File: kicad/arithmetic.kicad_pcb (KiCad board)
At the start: 4 copper layers, 47.3 x 58.3 mm, 72 parts, among them J1 Conn_01x03_Male, J2 Conn_01x05_Male, J3 Conn_01x05_Male, J4 Conn_Coaxial, J5 Conn_Coaxial, J6 Conn_Coaxial, M2.5 MountingHole_2.7mm_M2.5_ISO73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, U1 LM317, U2 LM337, U3 OPA197xDBV, U4 OPA197xDBV, U5 OPA197xDBV

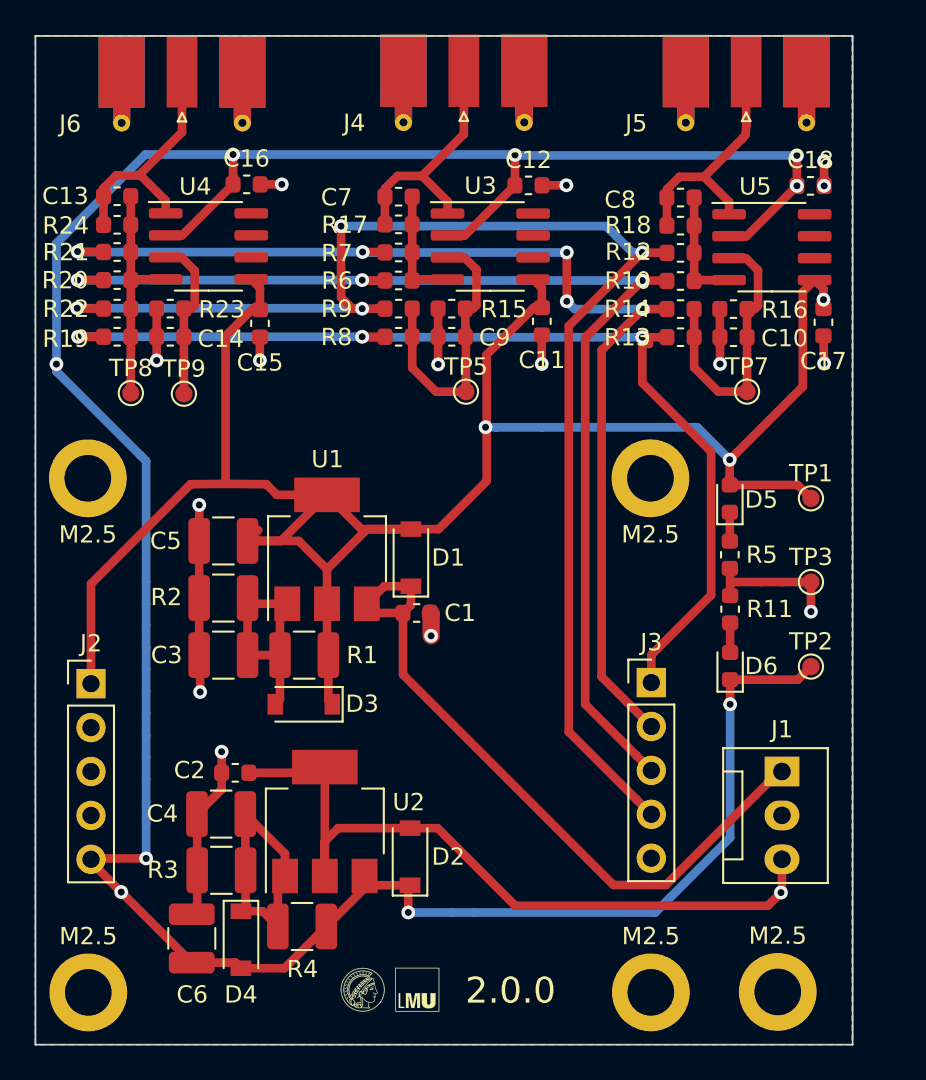
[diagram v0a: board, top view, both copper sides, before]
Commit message: fixed signal routing, remaining vias, large traces
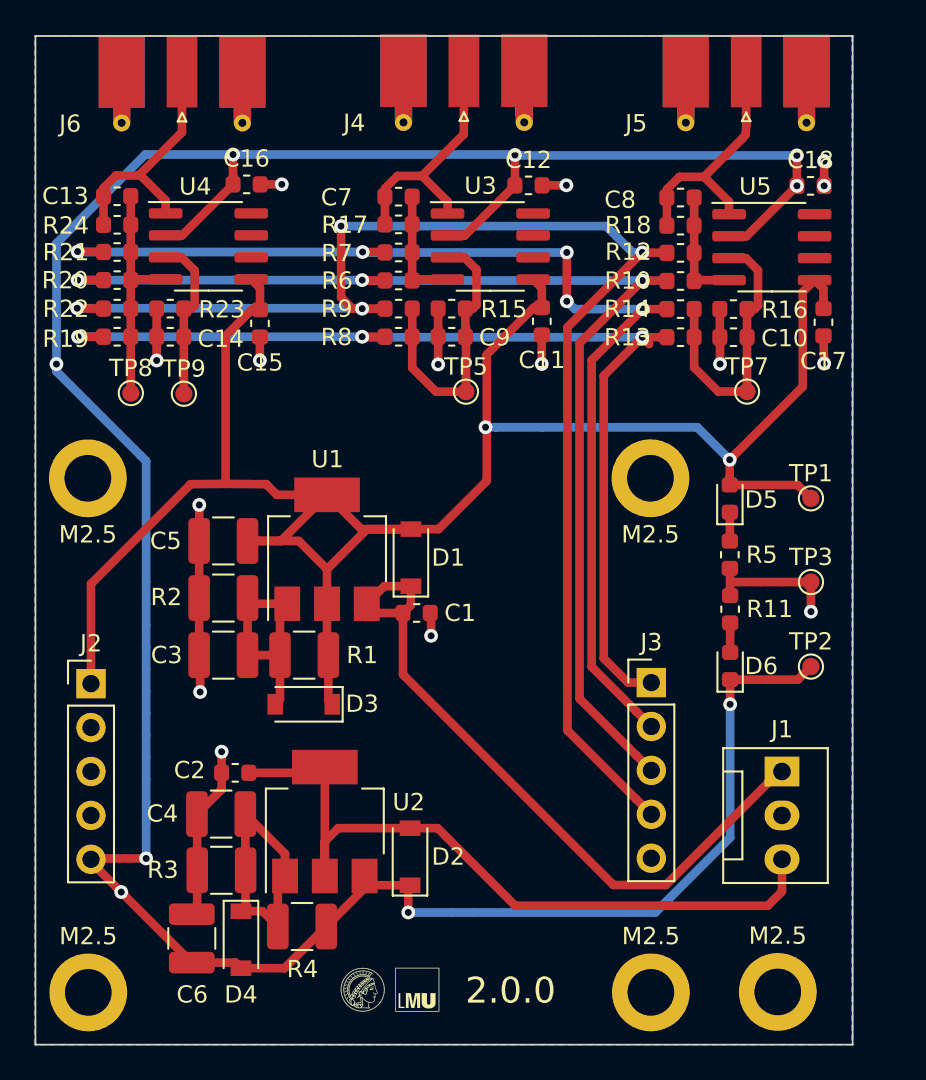
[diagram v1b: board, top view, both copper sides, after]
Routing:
- net +12V: track 121.3 -> 120.4 mm, vias 3 -> 2
- net -15V: vias 1 -> 0
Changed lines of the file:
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@@
     (thickness 1.6)
     (drawings 8)
-    (tracks 420)
+    (tracks 416)
     (zones 0)
     (modules 72)
@@
   )
   (setup
-    (last_trace_width 0.25)
+    (last_trace_width 0.5)
     (user_trace_width 0.5)
     (user_trace_width 0.75)
@@
   (segment (start 119.3806 86.1654) (end 119.3806 84.735) (width 0.5) (layer F.Cu) (net 1))
   (via (at 96.647 112.1918) (size 0.8) (drill 0.4) (layers F.Cu B.Cu) (net 1))
-  (segment (start 96.647 110.9217) (end 96.5963 110.871) (width 1) (layer F.Cu) (net 1))
-  (segment (start 96.647 112.1918) (end 96.647 110.9217) (width 1) (layer F.Cu) (net 1))
+  (segment (start 96.647 112.1918) (end 96.647 110.9217) (width 0.5) (layer F.Cu) (net 1))
+  (segment (start 96.647 110.9217) (end 96.5963 110.871) (width 0.5) (layer F.Cu) (net 1))
   (segment (start 119.3431 94.8429) (end 119.38 96.4438) (width 0.5) (layer F.Cu) (net 1))
   (segment (start 119.38 96.4438) (end 119.3431 96.4069) (width 0.5) (layer F.Cu) (net 1))
@@
   (segment (start 95.4278 123.318) (end 97.0278 123.318) (width 0.5) (layer F.Cu) (net 3))
   (segment (start 116.8835 127.0435) (end 116.9416 126.9854) (width 0.5) (layer F.Cu) (net 3))
-  (via (at 116.8835 127.0435) (size 0.8) (drill 0.4) (layers F.Cu B.Cu) (net 3))
   (segment (start 86.3608 110.3384) (end 86.0298 110.0074) (width 0.5) (layer F.Cu) (net 4))
   (segment (start 88.3272 110.3384) (end 86.3608 110.3384) (width 0.5) (layer F.Cu) (net 4))
@@
   (segment (start 90.7064 115.9296) (end 90.931 116.1542) (width 0.5) (layer F.Cu) (net 6))
   (segment (start 90.7064 113.3094) (end 90.7064 115.9296) (width 0.5) (layer F.Cu) (net 6))
-  (segment (start 86.0298 106.7054) (end 86.6548 106.0804) (width 0.5) (layer F.Cu) (net 6))
   (segment (start 86.6548 106.7054) (end 86.0298 106.7054) (width 0.5) (layer F.Cu) (net 6))
   (segment (start 88.9942 106.7054) (end 86.6548 106.7054) (width 0.5) (layer F.Cu) (net 6))
@@
   (segment (start 118.8324 91.6178) (end 118.143091 92.307109) (width 0.5) (layer F.Cu) (net 6))
   (segment (start 119.3431 92.7469) (end 119.3431 92.1285) (width 0.5) (layer F.Cu) (net 6))
-  (via (at 119.3431 92.7469) (size 0.8) (drill 0.4) (layers F.Cu B.Cu) (net 6))
   (segment (start 103.070601 100.129399) (end 100.403601 100.129399) (width 0.5) (layer B.Cu) (net 6))
   (segment (start 82.245 89.027) (end 81.2942 89.027) (width 0.5) (layer F.Cu) (net 7))
@@
   (segment (start 79.847716 85.56639) (end 78.42341 85.56639) (width 0.5) (layer F.Cu) (net 13))
   (segment (start 81.2942 87.757) (end 81.2942 87.012874) (width 0.5) (layer F.Cu) (net 13))
-  (segment (start 82.2392 79.54) (end 82.2392 83.064) (width 0.5) (layer F.Cu) (net 13) (status 1000000))
-  (segment (start 82.2392 83.064) (end 79.847716 85.455484) (width 0.5) (layer F.Cu) (net 13) (status 1000000))
-  (segment (start 79.847716 85.455484) (end 79.847716 85.56639) (width 0.5) (layer F.Cu) (net 13) (status 1000000))
+  (segment (start 82.2392 79.54) (end 82.2392 83.064) (width 0.5) (layer F.Cu) (net 13))
+  (segment (start 82.2392 83.064) (end 79.847716 85.455484) (width 0.5) (layer F.Cu) (net 13))
+  (segment (start 79.847716 85.455484) (end 79.847716 85.56639) (width 0.5) (layer F.Cu) (net 13))
   (segment (start 82.347 93.2688) (end 82.347 94.8944) (width 0.5) (layer F.Cu) (net 14))
   (segment (start 82.96921 93.08409) (end 82.7845 93.2688) (width 0.5) (layer F.Cu) (net 14))
@@
   (segment (start 108.8644 90.0176) (end 108.8898 90.043) (width 0.5) (layer F.Cu) (net 17))
   (via (at 108.8644 90.0176) (size 0.8) (drill 0.4) (layers F.Cu B.Cu) (net 17))
-  (segment (start 108.535101 121.666901) (end 109.3851 122.5169) (width 0.5) (layer F.Cu) (net 17))
-  (segment (start 104.609279 94.272721) (end 104.609279 117.741079) (width 0.5) (layer F.Cu) (net 17))
-  (segment (start 104.609279 117.741079) (end 108.535101 121.666901) (width 0.5) (layer F.Cu) (net 17))
-  (segment (start 108.8644 90.0176) (end 104.609279 94.272721) (width 0.5) (layer F.Cu) (net 17))
   (segment (start 93.9799 93.2688) (end 93.5424 93.2688) (width 0.5) (layer F.Cu) (net 17))
   (segment (start 93.5424 93.2688) (end 92.6592 93.2688) (width 0.5) (layer F.Cu) (net 17))
@@
   (segment (start 92.093515 93.2688) (end 92.6592 93.2688) (width 0.5) (layer F.Cu) (net 17))
   (segment (start 91.44 88.4936) (end 91.44 92.615285) (width 0.5) (layer F.Cu) (net 17))
+  (segment (start 108.535101 121.666901) (end 109.3851 122.5169) (width 0.5) (layer F.Cu) (net 17))
+  (segment (start 104.534269 117.666069) (end 108.535101 121.666901) (width 0.5) (layer F.Cu) (net 17))
+  (segment (start 104.534269 94.347731) (end 104.534269 117.666069) (width 0.5) (layer F.Cu) (net 17))
+  (segment (start 108.8644 90.0176) (end 104.534269 94.347731) (width 0.5) (layer F.Cu) (net 17))
   (segment (start 77.6985 89.9922) (end 76.2 89.9668) (width 0.5) (layer F.Cu) (net 18))
   (segment (start 76.2 89.9668) (end 76.2254 89.9922) (width 0.5) (layer F.Cu) (net 18))
@@
   (segment (start 108.8898 93.2942) (end 108.8898 93.2942) (width 0.5) (layer F.Cu) (net 18))
   (via (at 108.8898 93.2942) (size 0.8) (drill 0.4) (layers F.Cu B.Cu) (net 18))
-  (segment (start 108.489801 93.694199) (end 108.8898 93.2942) (width 0.5) (layer F.Cu) (net 18))
-  (segment (start 106.509299 95.674701) (end 108.489801 93.694199) (width 0.5) (layer F.Cu) (net 18))
-  (segment (start 106.509299 114.561099) (end 106.509299 95.674701) (width 0.5) (layer F.Cu) (net 18))
-  (segment (start 109.3851 117.4369) (end 106.509299 114.561099) (width 0.5) (layer F.Cu) (net 18))
   (segment (start 76.2254 89.9922) (end 76.2 89.9668) (width 0.5) (layer B.Cu) (net 18))
   (segment (start 92.6846 89.9922) (end 76.2254 89.9922) (width 0.5) (layer B.Cu) (net 18))
@@
   (segment (start 92.71 90.0176) (end 92.6846 89.9922) (width 0.5) (layer B.Cu) (net 18))
   (segment (start 104.4956 90.0176) (end 92.71 90.0176) (width 0.5) (layer B.Cu) (net 18))
+  (segment (start 108.535101 116.586901) (end 109.3851 117.4369) (width 0.5) (layer F.Cu) (net 18))
+  (segment (start 105.934289 113.986089) (end 108.535101 116.586901) (width 0.5) (layer F.Cu) (net 18))
+  (segment (start 105.934289 96.249711) (end 105.934289 113.986089) (width 0.5) (layer F.Cu) (net 18))
+  (segment (start 108.8898 93.2942) (end 105.934289 96.249711) (width 0.5) (layer F.Cu) (net 18))
   (segment (start 77.6985 91.6178) (end 77.261 91.6178) (width 0.5) (layer F.Cu) (net 19))
   (segment (start 77.261 91.6178) (end 76.2 91.6178) (width 0.5) (layer F.Cu) (net 19))
@@
   (segment (start 110.2612 91.6432) (end 110.2866 91.6686) (width 0.5) (layer F.Cu) (net 19))
   (segment (start 108.8644 91.6432) (end 110.2612 91.6432) (width 0.5) (layer F.Cu) (net 19))
-  (segment (start 108.535101 119.126901) (end 109.3851 119.9769) (width 0.5) (layer F.Cu) (net 19))
-  (segment (start 105.559289 116.151089) (end 108.535101 119.126901) (width 0.5) (layer F.Cu) (net 19))
-  (segment (start 105.559289 94.948311) (end 105.559289 116.151089) (width 0.5) (layer F.Cu) (net 19))
-  (segment (start 108.8644 91.6432) (end 105.559289 94.948311) (width 0.5) (layer F.Cu) (net 19))
   (segment (start 92.6846 91.6432) (end 92.6592 91.6178) (width 0.5) (layer B.Cu) (net 19))
   (segment (start 108.8644 91.6432) (end 92.6846 91.6432) (width 0.5) (layer B.Cu) (net 19))
   (segment (start 92.6592 91.6178) (end 76.2 91.6178) (width 0.5) (layer B.Cu) (net 19))
+  (segment (start 108.535101 119.126901) (end 109.3851 119.9769) (width 0.5) (layer F.Cu) (net 19))
+  (segment (start 105.234279 115.826079) (end 108.535101 119.126901) (width 0.5) (layer F.Cu) (net 19))
+  (segment (start 105.234279 95.273321) (end 105.234279 115.826079) (width 0.5) (layer F.Cu) (net 19))
+  (segment (start 108.8644 91.6432) (end 105.234279 95.273321) (width 0.5) (layer F.Cu) (net 19))
   (segment (start 77.6986 94.8944) (end 76.2254 94.8944) (width 0.5) (layer F.Cu) (net 20))
   (segment (start 76.2254 94.8944) (end 76.2254 94.8944) (width 0.5) (layer F.Cu) (net 20))
@@
   (via (at 76.2254 94.8944) (size 0.8) (drill 0.4) (layers F.Cu B.Cu) (net 20))
   (segment (start 92.6592 94.8944) (end 76.2254 94.8944) (width 0.5) (layer B.Cu) (net 20))
-  (segment (start 109.3851 113.2969) (end 109.3851 114.8969) (width 0.5) (layer F.Cu) (net 20))
-  (segment (start 112.84399 109.83801) (end 109.3851 113.2969) (width 0.5) (layer F.Cu) (net 20))
-  (segment (start 112.84399 101.54099) (end 112.84399 109.83801) (width 0.5) (layer F.Cu) (net 20))
-  (segment (start 108.8644 97.5614) (end 112.84399 101.54099) (width 0.5) (layer F.Cu) (net 20))
-  (segment (start 108.8644 94.9198) (end 108.8644 97.5614) (width 0.5) (layer F.Cu) (net 20))
+  (segment (start 108.0351 114.8969) (end 109.3851 114.8969) (width 0.5) (layer F.Cu) (net 20))
+  (segment (start 106.634299 113.496099) (end 108.0351 114.8969) (width 0.5) (layer F.Cu) (net 20))
+  (segment (start 106.634299 97.149901) (end 106.634299 113.496099) (width 0.5) (layer F.Cu) (net 20))
+  (segment (start 108.8644 94.9198) (end 106.634299 97.149901) (width 0.5) (layer F.Cu) (net 20))
   (segment (start 95.5522 86.7918) (end 95.5522 91.64) (width 0.5) (layer F.Cu) (net 21))
   (segment (start 95.6172 91.575) (end 95.5522 91.64) (width 0.5) (layer F.Cu) (net 21))

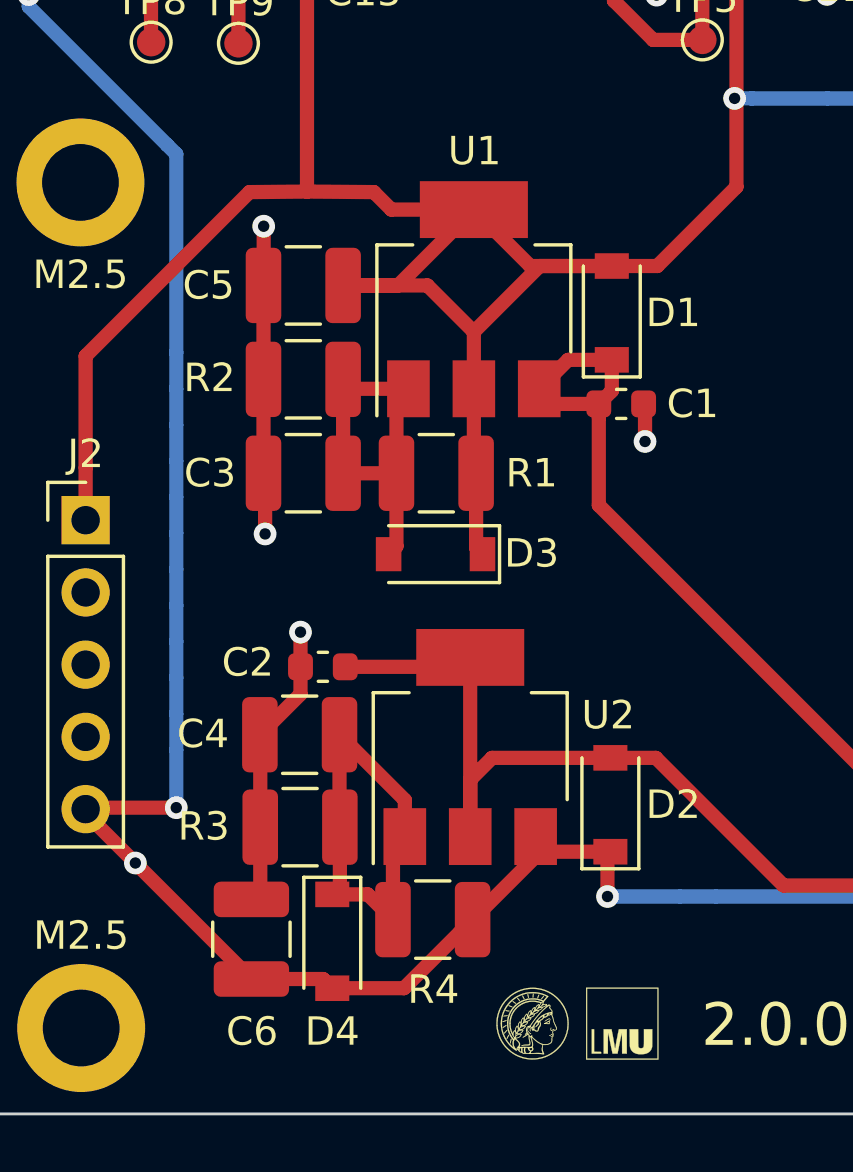
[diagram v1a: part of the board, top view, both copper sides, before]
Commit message: added fill zones around voltage regulators
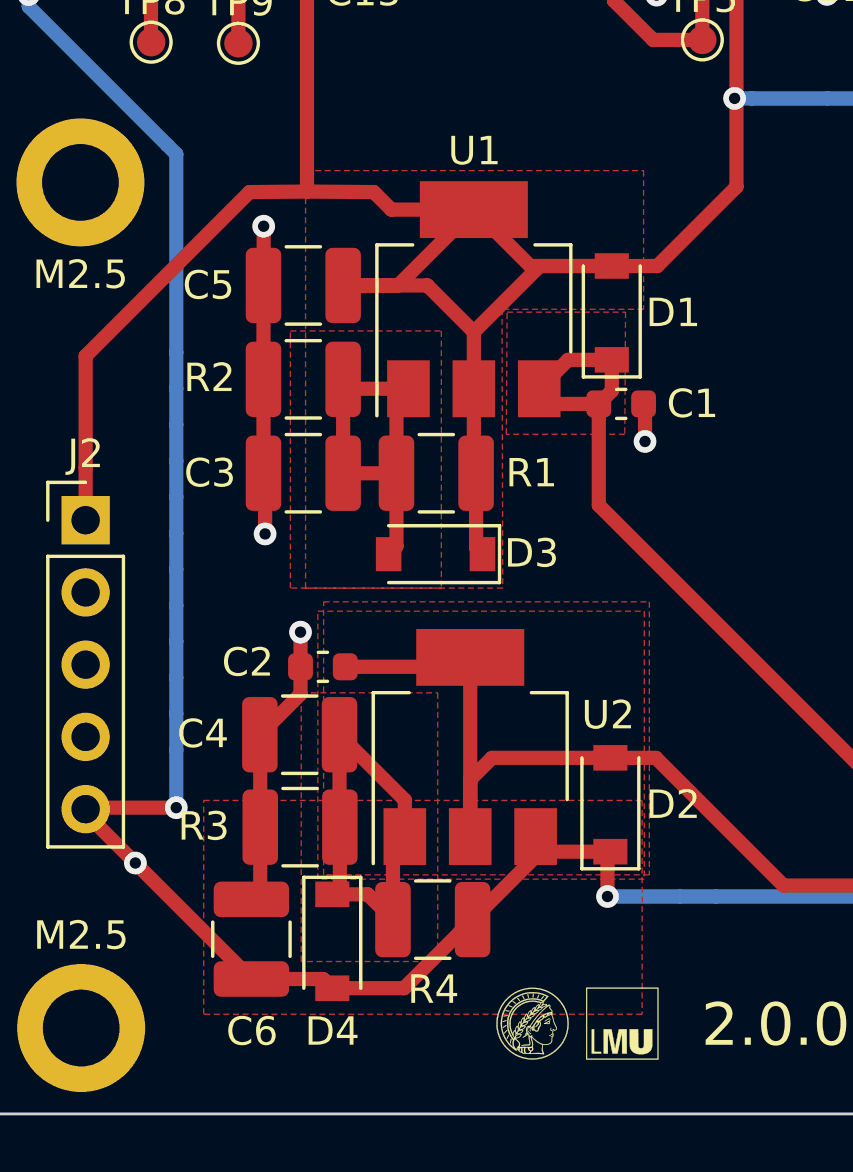
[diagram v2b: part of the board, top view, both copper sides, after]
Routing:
- added copper zone on F.Cu, net +12V
- added copper zone on F.Cu, net +15V
- added copper zone on F.Cu, net -12V
- added copper zone on F.Cu, net -15V
- added copper zone on F.Cu, net Net-(C3-Pad1)
- added copper zone on F.Cu, net Net-(C4-Pad2)
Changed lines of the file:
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@@
   )
   (setup
-    (last_trace_width 0.5)
+    (last_trace_width 0.75)
     (user_trace_width 0.5)
     (user_trace_width 0.75)
@@
     (connect_pads (clearance 0.508))
     (min_thickness 0.254)
-    (fill (arc_segments 32) (thermal_gap 0.508) (thermal_bridge_width 0.508))
+    (fill yes (arc_segments 32) (thermal_gap 0.508) (thermal_bridge_width 0.508))
     (polygon
       (pts
@@
     (connect_pads (clearance 0.508))
     (min_thickness 0.254)
-    (fill (arc_segments 32) (thermal_gap 0.508) (thermal_bridge_width 0.508))
+    (fill yes (arc_segments 32) (thermal_gap 0.508) (thermal_bridge_width 0.508))
     (polygon
       (pts
@@
     (connect_pads (clearance 0.508))
     (min_thickness 0.254)
-    (fill (arc_segments 32) (thermal_gap 0.508) (thermal_bridge_width 0.508))
+    (fill yes (arc_segments 32) (thermal_gap 0.508) (thermal_bridge_width 0.508))
     (polygon
       (pts
@@
     (connect_pads (clearance 0.508))
     (min_thickness 0.254)
-    (fill (arc_segments 32) (thermal_gap 0.508) (thermal_bridge_width 0.508))
+    (fill yes (arc_segments 32) (thermal_gap 0.508) (thermal_bridge_width 0.508))
     (polygon
       (pts
@@
       )
     )
+  )
+  (zone (net 4) (net_name "Net-(C3-Pad1)") (layer F.Cu) (hatch edge 0.508)
+    (priority 20)
+    (connect_pads (clearance 0.508))
+    (min_thickness 0.254)
+    (fill yes (arc_segments 32) (thermal_gap 0.508) (thermal_bridge_width 0.508))
+    (polygon
+      (pts
+        (xy 89.4842 117.348) (xy 84.1756 117.348) (xy 84.1756 108.3056) (xy 89.4842 108.3056)
+      )
+    )
+  )
+  (zone (net 2) (net_name +15V) (layer F.Cu) (hatch edge 0.508)
+    (priority 30)
+    (connect_pads (clearance 0.508))
+    (min_thickness 0.254)
+    (fill yes (arc_segments 32) (thermal_gap 0.508) (thermal_bridge_width 0.508))
+    (polygon
+      (pts
+        (xy 95.9358 111.9378) (xy 91.7702 111.9378) (xy 91.7956 107.6452) (xy 95.9612 107.6452)
+      )
+    )
+  )
+  (zone (net 6) (net_name +12V) (layer F.Cu) (hatch edge 0.508)
+    (priority 5)
+    (connect_pads (clearance 0.508))
+    (min_thickness 0.254)
+    (fill yes (arc_segments 32) (thermal_gap 0.508) (thermal_bridge_width 0.508))
+    (polygon
+      (pts
+        (xy 96.5962 107.5436) (xy 91.6178 107.5436) (xy 91.6432 117.348) (xy 84.709 117.348) (xy 84.709 102.6668)
+        (xy 96.5962 102.6668)
+      )
+    )
+  )
+  (zone (net 5) (net_name "Net-(C4-Pad2)") (layer F.Cu) (hatch edge 0.508)
+    (priority 20)
+    (connect_pads (clearance 0.508))
+    (min_thickness 0.254)
+    (fill yes (arc_segments 32) (thermal_gap 0.508) (thermal_bridge_width 0.508))
+    (polygon
+      (pts
+        (xy 89.3572 130.4798) (xy 84.5566 130.4798) (xy 84.5566 121.031) (xy 89.3572 121.031)
+      )
+    )
+  )
+  (zone (net 7) (net_name -12V) (layer F.Cu) (hatch edge 0.508)
+    (priority 20)
+    (connect_pads (clearance 0.508))
+    (min_thickness 0.254)
+    (fill yes (arc_segments 32) (thermal_gap 0.508) (thermal_bridge_width 0.508))
+    (polygon
+      (pts
+        (xy 96.5454 132.334) (xy 81.1276 132.334) (xy 81.1276 124.8156) (xy 96.5454 124.8156)
+      )
+    )
+  )
+  (zone (net 3) (net_name -15V) (layer F.Cu) (hatch edge 0.508)
+    (priority 5)
+    (connect_pads (clearance 0.508))
+    (min_thickness 0.254)
+    (fill yes (arc_segments 32) (thermal_gap 0.508) (thermal_bridge_width 0.508))
+    (polygon
+      (pts
+        (xy 96.6216 127.5842) (xy 85.1408 127.5842) (xy 85.1408 118.1608) (xy 96.6216 118.1608)
+      )
+    )
+  )
+  (zone (net 3) (net_name -15V) (layer F.Cu) (hatch edge 0.508)
+    (priority 5)
+    (connect_pads (clearance 0.508))
+    (min_thickness 0.254)
+    (fill yes (arc_segments 32) (thermal_gap 0.508) (thermal_bridge_width 0.508))
+    (polygon
+      (pts
+        (xy 96.7994 127.4318) (xy 85.344 127.4318) (xy 85.344 117.8306) (xy 96.7994 117.8306)
+      )
+    )
